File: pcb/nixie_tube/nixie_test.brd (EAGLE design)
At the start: 100 x 80 mm, 17 parts, among them IC1 74141N

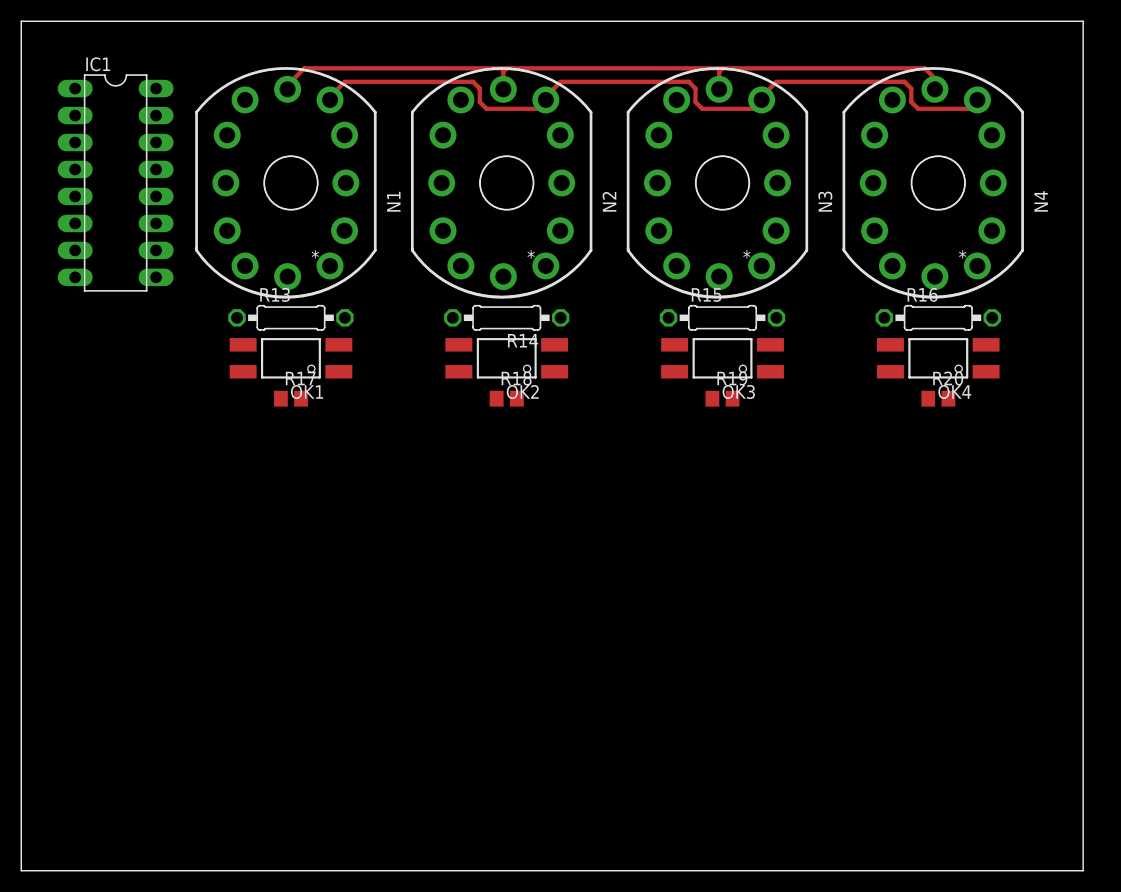
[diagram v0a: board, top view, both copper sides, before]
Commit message: 
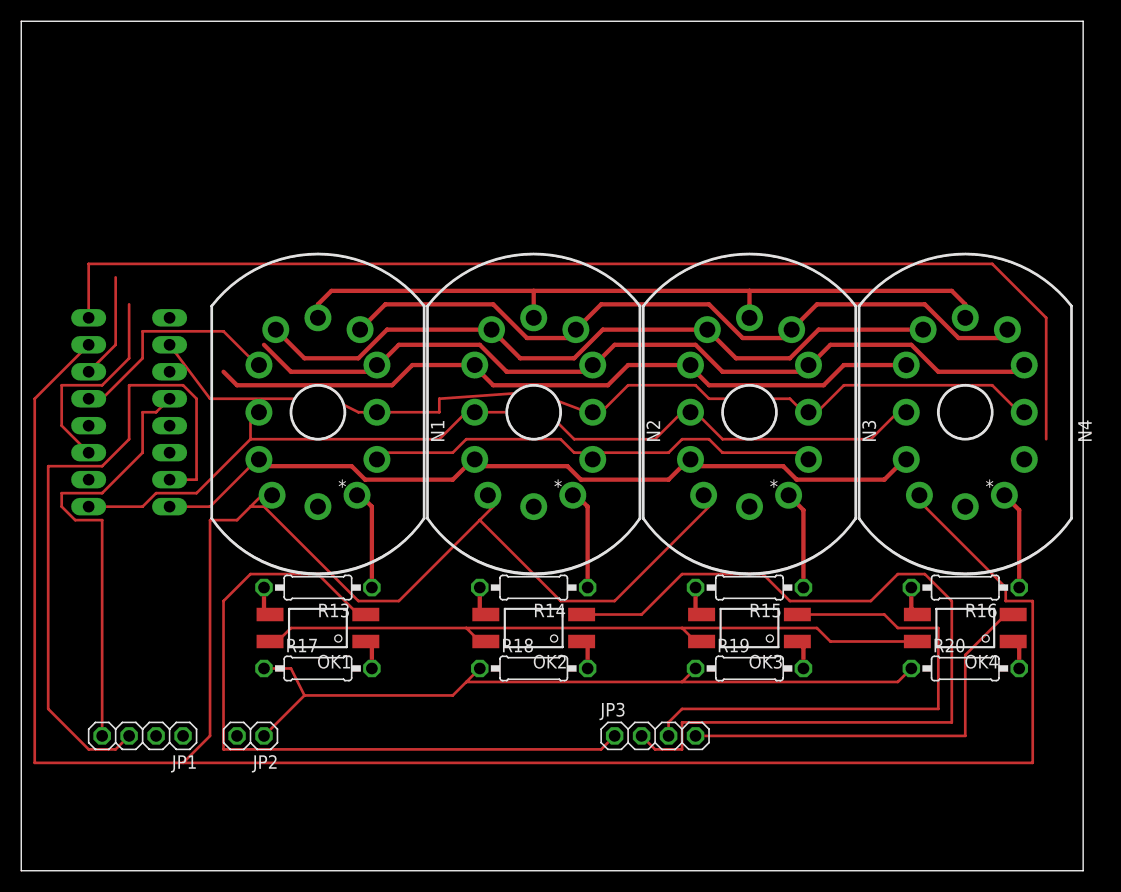
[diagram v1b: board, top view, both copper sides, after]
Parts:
- added JP1, JP3: (no value), nixie_tube:1X04
- added JP2: (no value), nixie_tube:1X02
- R17, R18, R19, R20: device nixie_tube:R0805 -> nixie_tube:0207/10
- moved R17 25.5 mm to (27.9, 19.1)
- moved R18 25.5 mm to (48.3, 19.1)
- moved R19 25.5 mm to (68.6, 19.1)
- moved R20 25.5 mm to (88.9, 19.1)
- moved OK1 25.5 mm to (27.9, 22.9)
- moved OK2 25.5 mm to (48.3, 22.9)
- moved OK3 25.5 mm to (68.6, 22.9)
- moved OK4 25.5 mm to (88.9, 22.9)
- moved R13 25.5 mm to (27.9, 26.7), turned to 180 degrees
- moved R14 25.5 mm to (48.3, 26.7)
- moved R15 25.5 mm to (68.6, 26.7), turned to 180 degrees
- moved R16 25.5 mm to (88.9, 26.7), turned to 180 degrees
- moved N1 21.7 mm to (27.9, 43.2)
- moved N2 21.7 mm to (48.3, 43.2)
- moved N3 21.7 mm to (68.6, 43.2)
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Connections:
- new net A1: JP3.1, OK1.2
- new net A2: JP3.2, OK2.2
- new net A3: JP3.3, OK3.2
- new net A4: JP3.4, OK4.2
- new net N$1: IC1.3, JP1.1
- new net N$2: IC1.6, JP1.2
- new net N$3: IC1.7, JP1.3
- new net N$4: IC1.4, JP1.4
- net +5V: now also JP2.1
- net GND: now also JP2.2
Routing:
- net C1: track 0.00 -> 258.3 mm
- net C0: track 0.00 -> 152.6 mm
- net C4: track 0.00 -> 90.5 mm
- net C9: track 0.00 -> 89.2 mm
- net C3: track 0.00 -> 88.2 mm
- net A2: track 0.00 -> 83.3 mm
- net C8: track 0.00 -> 80.3 mm
- net C5: track 0.00 -> 77.6 mm
- net C2: track 0.00 -> 75.2 mm
- net +5V: track 0.00 -> 72.6 mm
- net A1: track 0.00 -> 67.4 mm
- net +24V: track 0.00 -> 66.7 mm
- net N$3: track 0.00 -> 63.4 mm
- net A3: track 0.00 -> 48.6 mm
- net N$4: track 0.00 -> 42.0 mm
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
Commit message: 
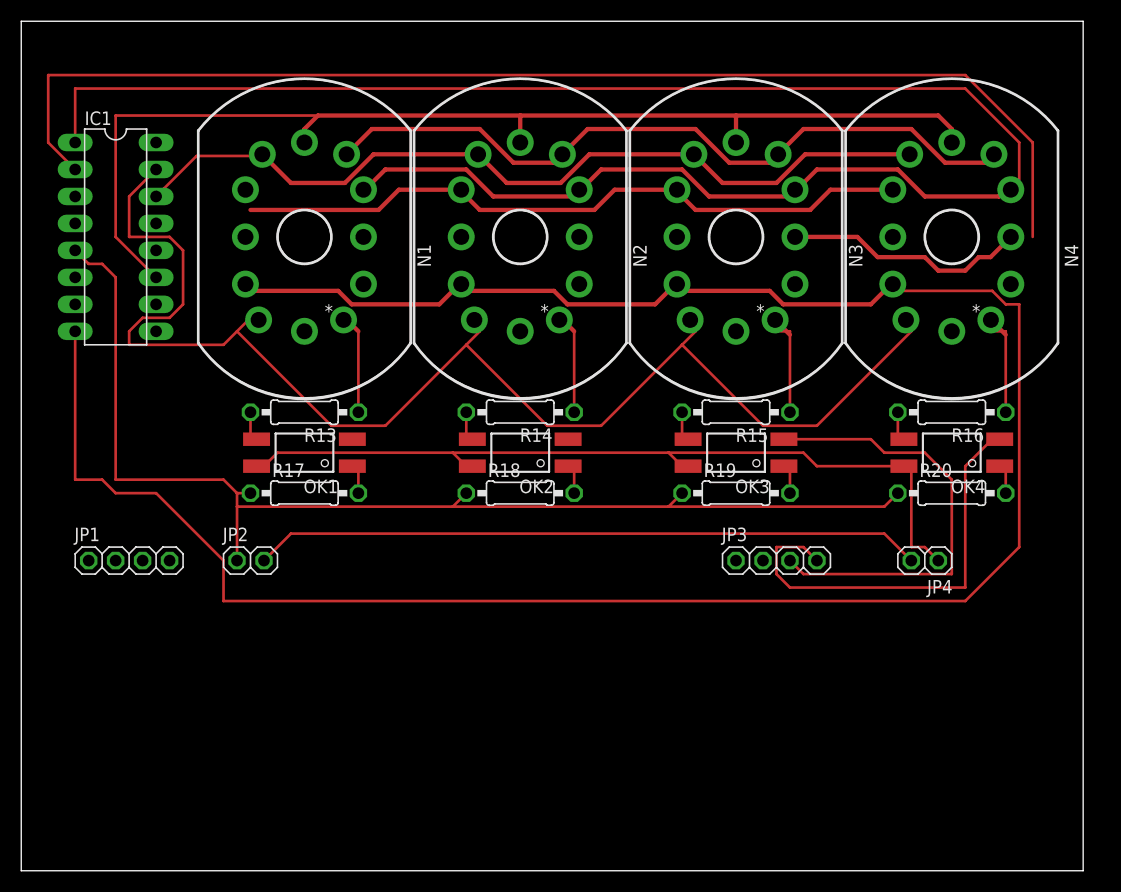
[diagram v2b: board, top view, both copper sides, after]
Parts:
- added JP4: (no value), nixie_tube:1X02
- moved JP3 20.1 mm to (71.1, 29.2)
- moved JP1 16.6 mm to (10.2, 29.2), turned to 0 degrees
- moved R17 16.6 mm to (26.7, 35.6)
- moved R18 16.6 mm to (47.0, 35.6)
- moved R19 16.6 mm to (67.3, 35.6)
- moved R20 16.6 mm to (87.6, 35.6)
- moved IC1 16.6 mm to (8.89, 59.7), flipped to the top
- moved N1 16.6 mm to (26.7, 59.7)
- moved N2 16.6 mm to (47.0, 59.7)
- moved N3 16.6 mm to (67.3, 59.7)
- moved N4 16.6 mm to (87.6, 59.7)
- moved OK1 16.6 mm to (26.7, 39.4)
- moved OK2 16.6 mm to (47.0, 39.4)
- moved OK3 16.6 mm to (67.3, 39.4)
- moved OK4 16.6 mm to (87.6, 39.4)
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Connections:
- net +24V: now also JP4.1
- net GND: now also JP4.2
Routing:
- net C0: track 152.6 -> 0.00 mm
- net C2: track 75.2 -> 215.4 mm
- net C1: track 258.3 -> 129.4 mm
- net C8: track 80.3 -> 169.3 mm
- net C3: track 88.2 -> 0.00 mm
- net A2: track 83.3 -> 0.00 mm
- net A1: track 67.4 -> 0.00 mm
- net N$3: track 63.4 -> 0.00 mm
- net GND: track 0.00 -> 63.1 mm
- net C9: track 89.2 -> 137.1 mm
- net N$4: track 42.0 -> 0.00 mm
- net +5V: track 72.6 -> 109.8 mm
- net C4: track 90.5 -> 64.7 mm
- net C6: track 89.5 -> 105.5 mm
- net +24V: track 66.7 -> 78.1 mm
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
